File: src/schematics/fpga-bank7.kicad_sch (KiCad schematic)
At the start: 5 parts, among them U6 LFE5U-85F-*BG756*

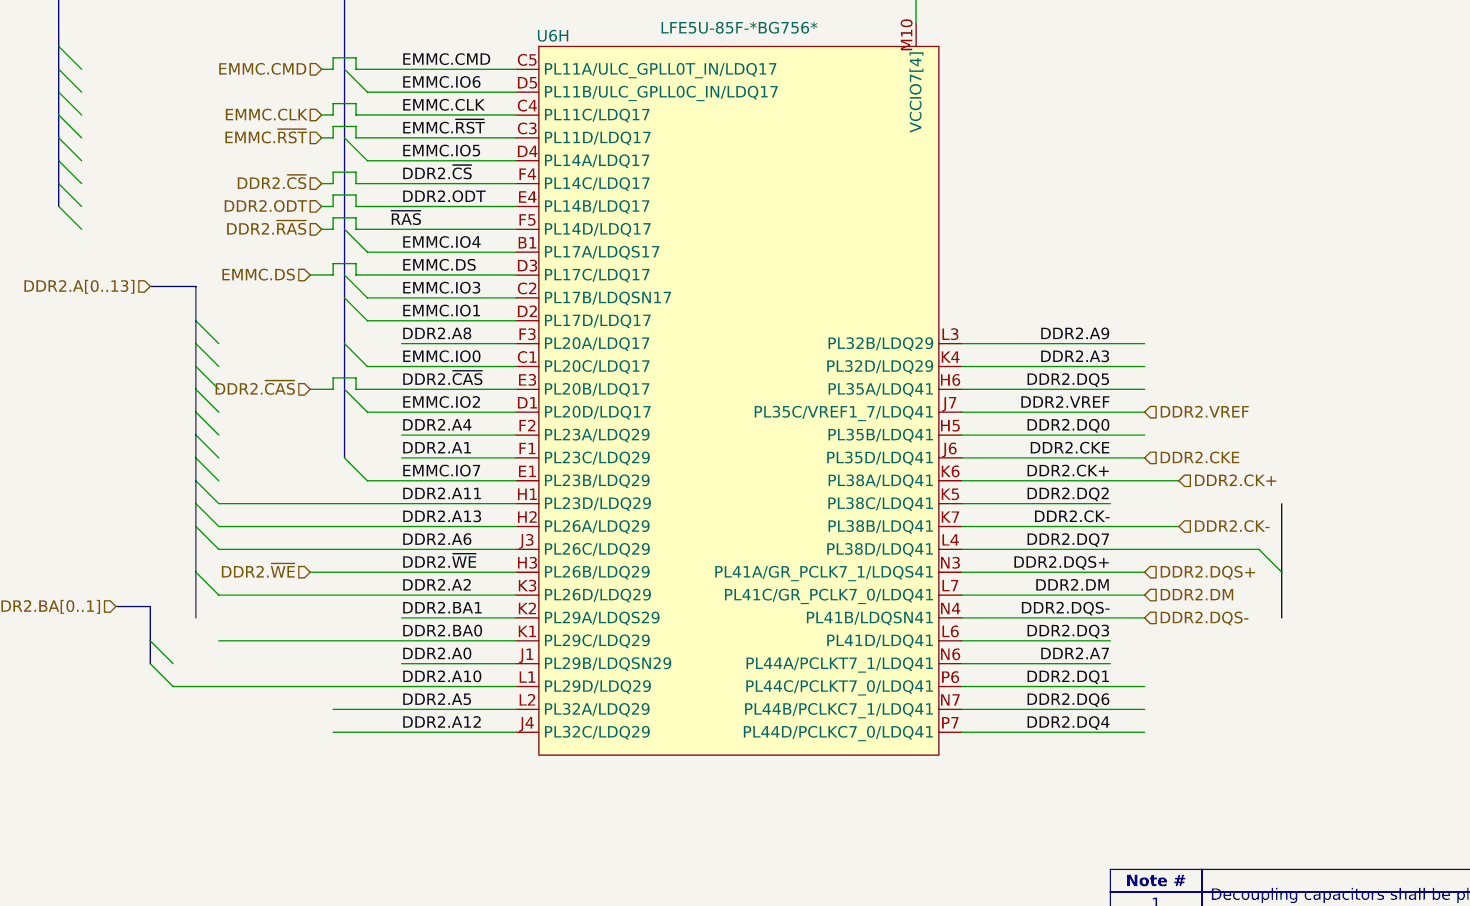
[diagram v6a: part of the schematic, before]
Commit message: Route the DDR2 without length matching
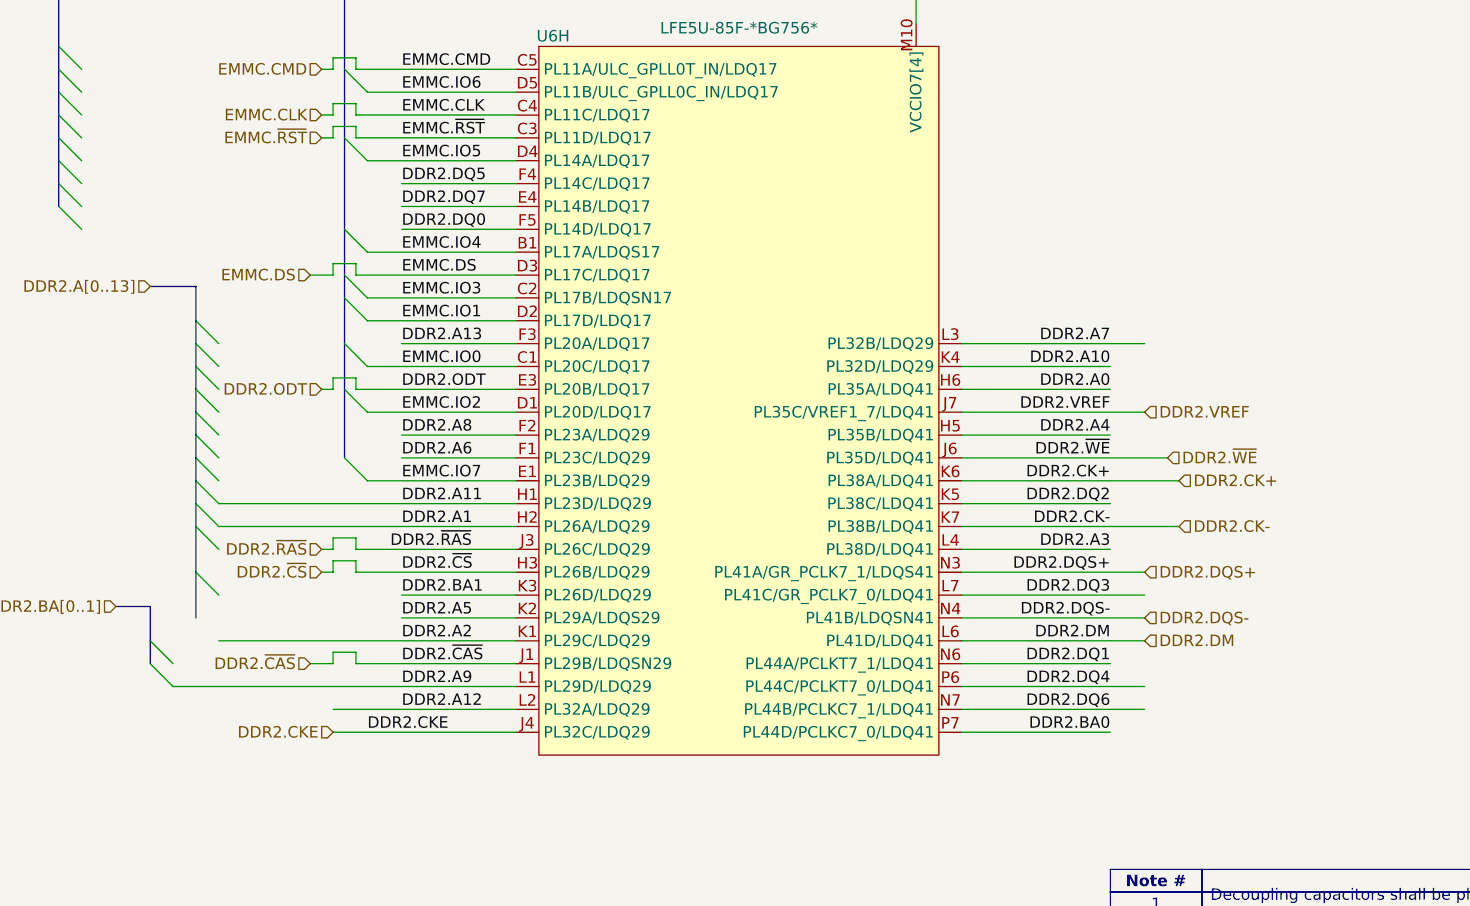
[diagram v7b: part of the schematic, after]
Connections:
- net DDR2.A0: now also U6.H6 (PL35A/LDQ41); no longer U6.J1 (PL29B/LDQSN29)
- net DDR2.A1: now also U6.H2 (PL26A/LDQ29); no longer U6.F1 (PL23C/LDQ29)
- net DDR2.A10: now also U6.K4 (PL32D/LDQ29); no longer U6.L1 (PL29D/LDQ29)
- net DDR2.A12: now also U6.L2 (PL32A/LDQ29); no longer U6.J4 (PL32C/LDQ29)
- net DDR2.A13: now also U6.F3 (PL20A/LDQ17); no longer U6.H2 (PL26A/LDQ29)
- net DDR2.A2: now also U6.K1 (PL29C/LDQ29); no longer U6.K3 (PL26D/LDQ29)
- net DDR2.A3: now also U6.L4 (PL38D/LDQ41); no longer U6.K4 (PL32D/LDQ29)
- net DDR2.A4: now also U6.H5 (PL35B/LDQ41); no longer U6.F2 (PL23A/LDQ29)
- net DDR2.A5: now also U6.K2 (PL29A/LDQS29); no longer U6.L2 (PL32A/LDQ29)
- net DDR2.A6: now also U6.F1 (PL23C/LDQ29); no longer U6.J3 (PL26C/LDQ29)
- net DDR2.A7: now also U6.L3 (PL32B/LDQ29); no longer U6.N6 (PL44A/PCLKT7_1/LDQ41)
- net DDR2.A8: now also U6.F2 (PL23A/LDQ29); no longer U6.F3 (PL20A/LDQ17)
- net DDR2.A9: now also U6.L1 (PL29D/LDQ29); no longer U6.L3 (PL32B/LDQ29)
- net DDR2.BA0: now also U6.P7 (PL44D/PCLKC7_0/LDQ41); no longer U6.K1 (PL29C/LDQ29)
- net DDR2.BA1: now also U6.K3 (PL26D/LDQ29); no longer U6.K2 (PL29A/LDQS29)
- net DDR2.CKE: now also U6.J4 (PL32C/LDQ29); no longer U6.J6 (PL35D/LDQ41)
- net DDR2.DM: now also U6.L6 (PL41D/LDQ41); no longer U6.L7 (PL41C/GR_PCLK7_0/LDQ41)
- net DDR2.DQ0: now also U6.F5 (PL14D/LDQ17); no longer U6.H5 (PL35B/LDQ41)
- net DDR2.DQ1: now also U6.N6 (PL44A/PCLKT7_1/LDQ41); no longer U6.P6 (PL44C/PCLKT7_0/LDQ41)
- net DDR2.DQ3: now also U6.L7 (PL41C/GR_PCLK7_0/LDQ41); no longer U6.L6 (PL41D/LDQ41)
- net DDR2.DQ4: now also U6.P6 (PL44C/PCLKT7_0/LDQ41); no longer U6.P7 (PL44D/PCLKC7_0/LDQ41)
- net DDR2.DQ5: now also U6.F4 (PL14C/LDQ17); no longer U6.H6 (PL35A/LDQ41)
- net DDR2.DQ7: now also U6.E4 (PL14B/LDQ17); no longer U6.L4 (PL38D/LDQ41)
- net DDR2.ODT: now also U6.E3 (PL20B/LDQ17); no longer U6.E4 (PL14B/LDQ17)
- net DDR2.~{CAS}: now also U6.J1 (PL29B/LDQSN29); no longer U6.E3 (PL20B/LDQ17)
- net DDR2.~{CS}: now also U6.H3 (PL26B/LDQ29); no longer U6.F4 (PL14C/LDQ17)
- net DDR2.~{RAS}: now also U6.J3 (PL26C/LDQ29); no longer U6.F5 (PL14D/LDQ17)
- net DDR2.~{WE}: now also U6.J6 (PL35D/LDQ41); no longer U6.H3 (PL26B/LDQ29)

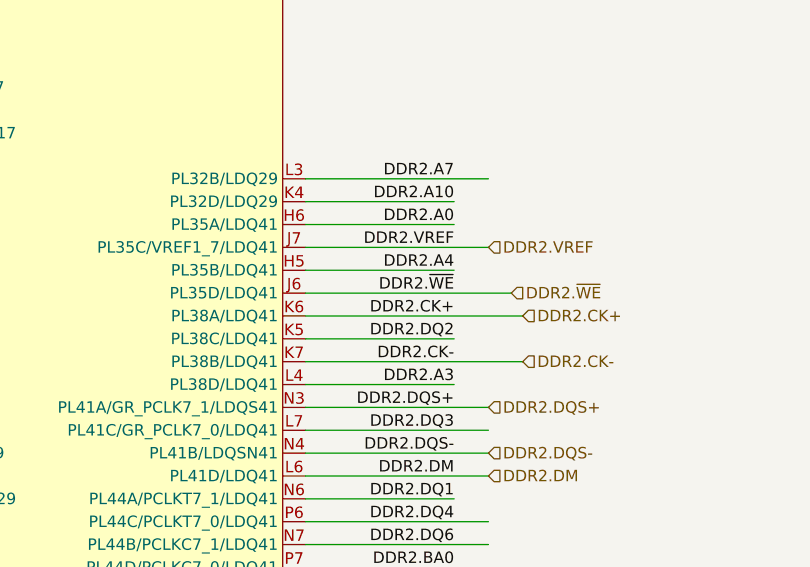
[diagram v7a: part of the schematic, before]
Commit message: Add length matching for DDR on L4 and L6. Todo L1 and redo L6
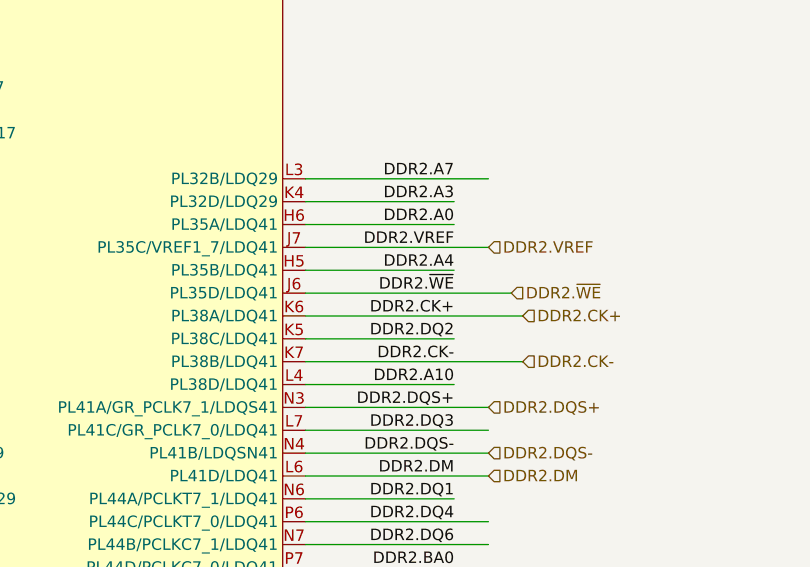
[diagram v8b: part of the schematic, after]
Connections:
- net DDR2.A10: now also U6.L4 (PL38D/LDQ41); no longer U6.K4 (PL32D/LDQ29)
- net DDR2.A3: now also U6.K4 (PL32D/LDQ29); no longer U6.L4 (PL38D/LDQ41)
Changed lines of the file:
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@@
 	)
 	(label "DDR2.A3"
-		(at 193.04 127 180)
+		(at 193.04 106.68 180)
 		(effects
 			(font
@@
 	)
 	(label "DDR2.A10"
-		(at 193.04 106.68 180)
-		(effects
-			(font
+		(at 193.04 127 180)
+		(effects
+			(font
